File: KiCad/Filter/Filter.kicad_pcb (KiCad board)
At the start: 2 copper layers, 51 x 59 mm, 36 parts, among them J1 Screw_Terminal_01x03, J2 Screw_Terminal_01x03, U1 TL074

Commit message: added silkscreen to help assembly process on all boards
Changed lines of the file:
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@@
 		)
 		(property "Value" "1k"
-			(at 3.81 2.37 0)
+			(at 2 -0.5 0)
 			(layer "F.Fab")
 			(effects
@@
 		)
 		(fp_text user "${REFERENCE}"
-			(at 3.81 0 0)
+			(at 5.5 0.5 0)
 			(layer "F.Fab")
 			(effects
@@
 		(tags "C Rect series Radial pin pitch 15.00mm length 18mm width 5mm Capacitor")
 		(property "Reference" "C3"
-			(at -0.9 -3.75 90)
+			(at -1.15 -3.8 180)
 			(layer "F.SilkS")
 			(effects
@@
 		)
 		(property "Value" "1n"
-			(at 7.5 3.75 90)
-			(layer "F.Fab")
+			(at 7.5 0.2 180)
+			(layer "F.SilkS")
 			(effects
 				(font
@@
 		)
 		(property "Value" "1n"
-			(at 4.5 0 0)
-			(layer "F.Fab")
+			(at 7.5 0 0)
+			(layer "F.SilkS")
 			(effects
 				(font
@@
 		(tags "THT DIP DIL PDIP 2.54mm 7.62mm 300mil")
 		(property "Reference" "U1"
-			(at 3.81 -2.33 90)
+			(at 3.805 -2.63 180)
 			(layer "F.SilkS")
 			(effects
@@
 		)
 		(property "Value" "TL074"
-			(at 3.81 17.57 90)
-			(layer "F.Fab")
+			(at 3.81 7.62 180)
+			(layer "F.SilkS")
 			(effects
 				(font
@@
 		)
 		(property "Value" "1n"
-			(at 7.5 3.75 0)
-			(layer "F.Fab")
+			(at 7.5 0 0)
+			(layer "F.SilkS")
 			(effects
 				(font

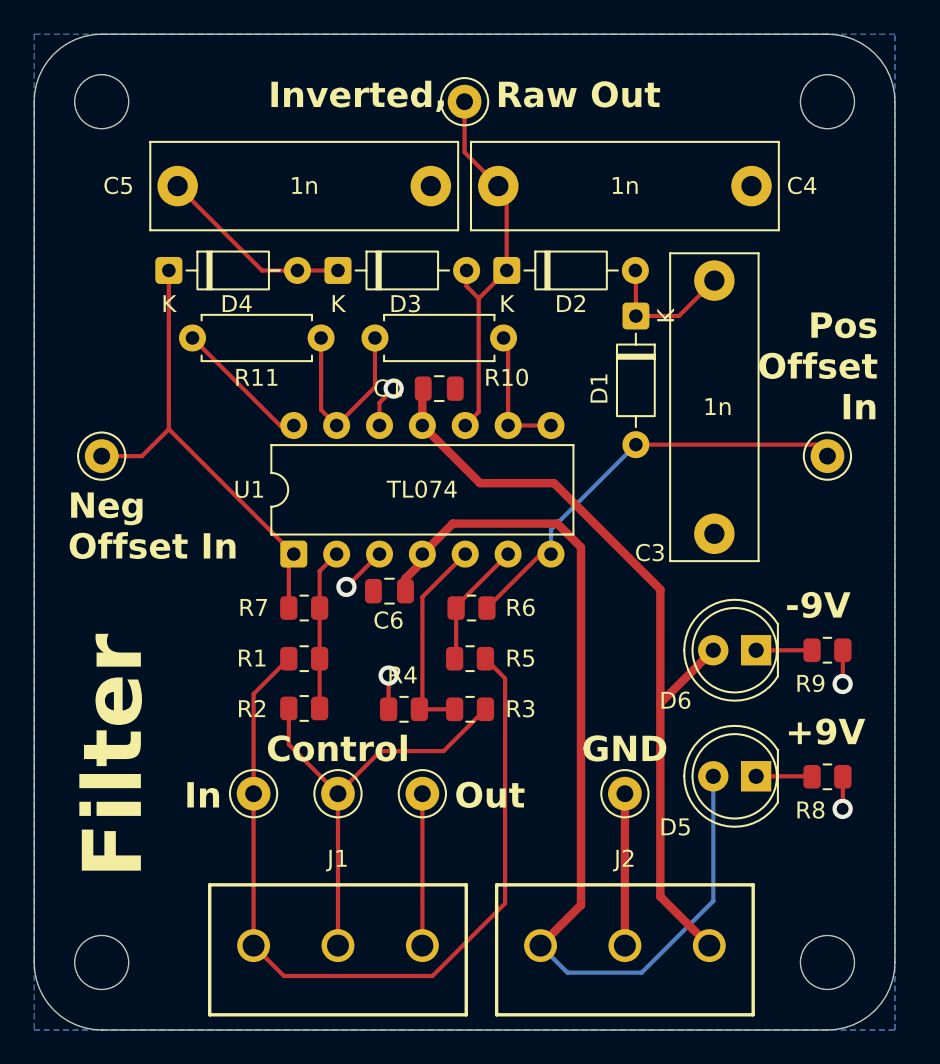
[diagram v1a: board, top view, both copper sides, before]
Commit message: ran DRC on all boards
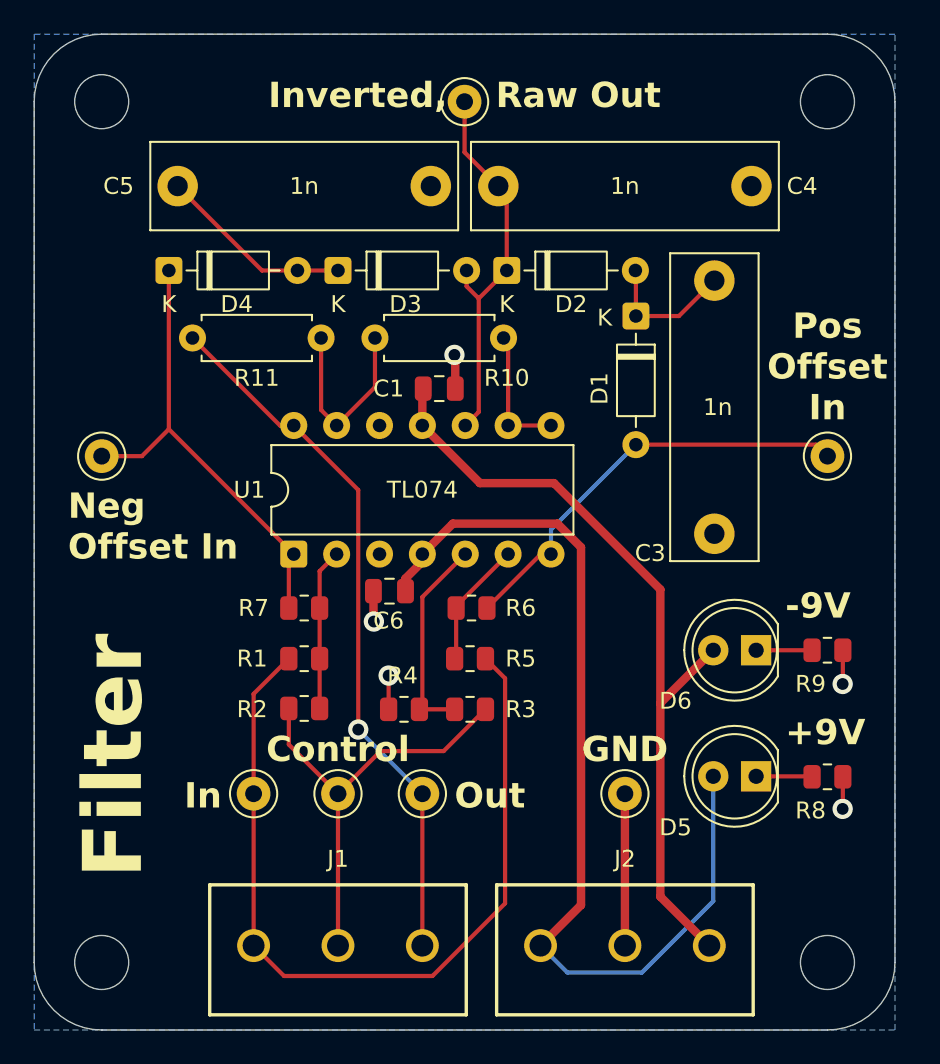
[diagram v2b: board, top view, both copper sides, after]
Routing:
- net /Out: track 17.1 -> 42.3 mm, vias 0 -> 1
- net GND: track 20.2 -> 18.7 mm
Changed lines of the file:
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@@
 			)
 		)
+		(property ki_fp_filters "MountingHole*")
+		(sheetname "/")
+		(sheetfile "Filter.kicad_sch")
+		(units
+			(unit
+				(name "A")
+				(pins)
+			)
+		)
 		(attr exclude_from_pos_files exclude_from_bom)
 		(duplicate_pad_numbers_are_jumpers no)
@@
 			)
 		)
+		(property ki_fp_filters "MountingHole*")
+		(sheetname "/")
+		(sheetfile "Filter.kicad_sch")
+		(units
+			(unit
+				(name "A")
+				(pins)
+			)
+		)
 		(attr exclude_from_pos_files exclude_from_bom)
 		(duplicate_pad_numbers_are_jumpers no)
@@
 			)
 		)
+		(property ki_fp_filters "MountingHole*")
+		(sheetname "/")
+		(sheetfile "Filter.kicad_sch")
+		(units
+			(unit
+				(name "A")
+				(pins)
+			)
+		)
 		(attr exclude_from_pos_files exclude_from_bom)
 		(duplicate_pad_numbers_are_jumpers no)
@@
 		)
 		(fp_text user "K"
-			(at 0 -1.8 90)
+			(at 0.1 1.85 180)
 			(layer "F.SilkS")
 			(effects
@@
 			)
 		)
+		(property ki_fp_filters "MountingHole*")
+		(sheetname "/")
+		(sheetfile "Filter.kicad_sch")
+		(units
+			(unit
+				(name "A")
+				(pins)
+			)
+		)
 		(attr exclude_from_pos_files exclude_from_bom)
 		(duplicate_pad_numbers_are_jumpers no)
@@
 	)
 	(gr_text "Pos\nOffset\nIn"
-		(at 117 67 0)
+		(at 114 67 0)
 		(layer "F.SilkS")
 		(effects
@@
 				(bold yes)
 			)
-			(justify right bottom)
+			(justify bottom)
 		)
 	)
@@
 	)
 	(segment
+		(start 86.2 71.005)
+		(end 82.38 67.185)
+		(width 0.25)
+		(layer "F.Cu")
+		(net "/Out")
+	)
+	(segment
 		(start 81.565 67.185)
 		(end 82.38 67.185)
@@
 	)
 	(segment
+		(start 86.2 85.2)
+		(end 86.2 71.005)
+		(width 0.25)
+		(layer "F.Cu")
+		(net "/Out")
+	)
+	(segment
+		(start 90 89)
+		(end 90.1 88.9)
+		(width 0.25)
+		(layer "F.Cu")
+		(net "/Out")
+	)
+	(segment
 		(start 90 98)
 		(end 90 89)
@@
 		(net "/Out")
 	)
+	(via
+		(at 86.2 85.2)
+		(size 1.2)
+		(drill 0.7)
+		(layers "F.Cu" "B.Cu")
+		(net "/Out")
+	)
+	(segment
+		(start 90 89)
+		(end 86.2 85.2)
+		(width 0.25)
+		(layer "B.Cu")
+		(net "/Out")
+	)
 	(segment
 		(start 94.9 95.5)
@@
 	)
 	(segment
-		(start 87.46 65.84)
-		(end 88.3 65)
-		(width 0.25)
+		(start 91.95 63.05)
+		(end 91.9 63)
+		(width 0.5)
 		(layer "F.Cu")
 		(net "GND")
@@
 	)
 	(segment
-		(start 87.46 67.185)
-		(end 87.46 65.84)
+		(start 114.9125 80.5)
+		(end 114.9125 82.4875)
 		(width 0.25)
 		(layer "F.Cu")
@@
 	)
 	(segment
-		(start 114.9125 80.5)
-		(end 114.9125 82.4875)
-		(width 0.25)
+		(start 91.95 65)
+		(end 91.95 63.05)
+		(width 0.5)
 		(layer "F.Cu")
 		(net "GND")
@@
 	)
 	(segment
-		(start 102 98)
-		(end 102 89)
+		(start 87.1 77)
+		(end 87.1 78.775)
 		(width 0.5)
 		(layer "F.Cu")
@@
 	)
 	(segment
-		(start 85.5 76.75)
-		(end 87.445 74.805)
-		(width 0.25)
+		(start 102 98)
+		(end 102 89)
+		(width 0.5)
 		(layer "F.Cu")
 		(net "GND")
@@
 	)
 	(segment
-		(start 87.445 74.805)
-		(end 87.46 74.805)
-		(width 0.25)
+		(start 87.1 78.775)
+		(end 87.125 78.8)
+		(width 0.5)
 		(layer "F.Cu")
 		(net "GND")
@@
 	)
 	(via
-		(at 85.5 76.75)
+		(at 91.9 63)
 		(size 1.2)
 		(drill 0.7)
@@
 	)
 	(via
-		(at 88 82)
+		(at 87.125 78.8)
 		(size 1.2)
 		(drill 0.7)
@@
 	)
 	(via
-		(at 88.3 65)
+		(at 88 82)
 		(size 1.2)
 		(drill 0.7)

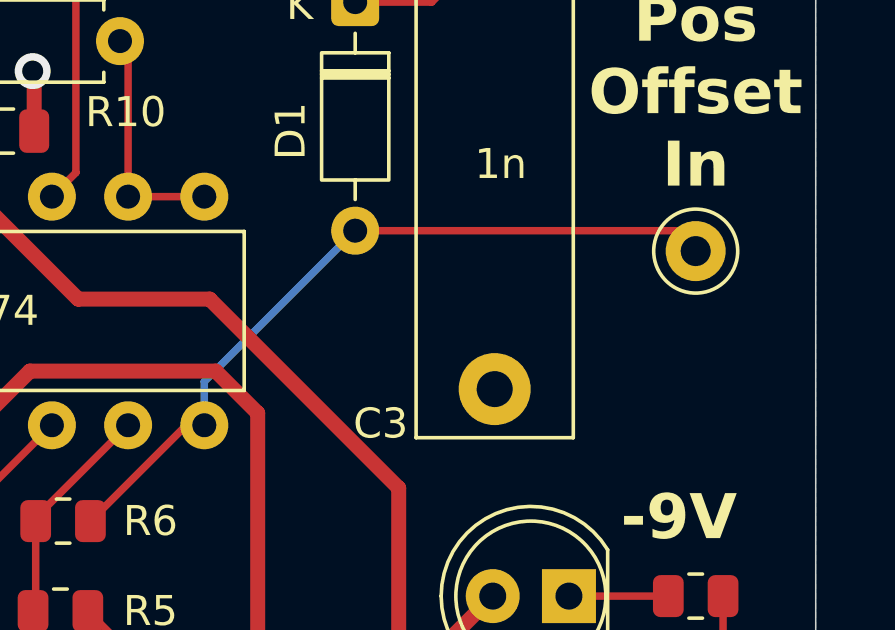
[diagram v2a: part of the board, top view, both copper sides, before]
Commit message: added protection resistor to diode ladder
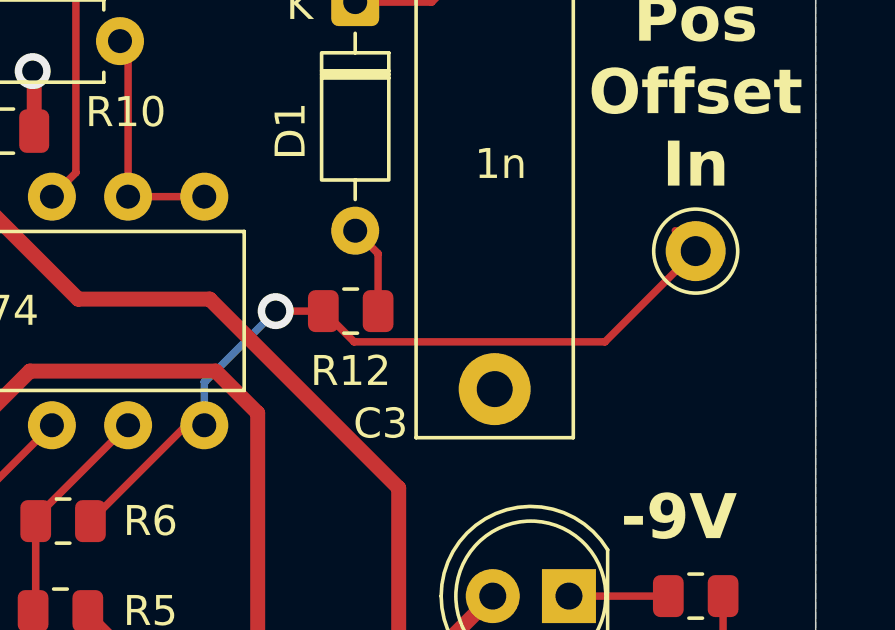
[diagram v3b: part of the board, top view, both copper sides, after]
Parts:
- added R12: 2.2k, Resistor_SMD:R_0805_2012Metric, F.Cu at (102.5, 71.0)
- H1, H2, H3, H4: value MountingHole_3.2mm_M3 -> MountingHole
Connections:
- D1 pad 2: /Signal w. + Offset -> Net-(D1-A)
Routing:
- net Net-(D1-A): track 0.00 -> 3.00 mm
- net /Signal w. + Offset: track 25.3 -> 26.6 mm, vias 0 -> 1
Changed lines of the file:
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@@
 			)
 		)
-		(property "Value" "MountingHole_3.2mm_M3"
+		(property "Value" "MountingHole"
 			(at 0 4.15 0)
 			(layer "F.Fab")
@@
 			)
 		)
-		(property "Description" ""
+		(property "Description" "Mounting Hole without connection"
 			(at 0 0 0)
 			(layer "F.Fab")
@@
 			)
 		)
-		(attr exclude_from_pos_files exclude_from_bom)
+		(attr exclude_from_bom)
 		(duplicate_pad_numbers_are_jumpers no)
 		(fp_circle
@@
 			)
 		)
-		(property "Value" "MountingHole_3.2mm_M3"
+		(property "Value" "MountingHole"
 			(at 0 4.15 0)
 			(layer "F.Fab")
@@
 			)
 		)
-		(property "Description" ""
+		(property "Description" "Mounting Hole without connection"
 			(at 0 0 0)
 			(layer "F.Fab")
@@
 			)
 		)
-		(attr exclude_from_pos_files exclude_from_bom)
+		(attr exclude_from_bom)
 		(duplicate_pad_numbers_are_jumpers no)
 		(fp_circle
@@
 		)
 	)
+	(footprint "Resistor_SMD:R_0805_2012Metric"
+		(layer "F.Cu")
+		(at 102.5 71)
+		(descr "Resistor SMD 0805 (2012 Metric), square (rectangular) end terminal, IPC-7351 nominal, (Body size source: IPC-SM-782 page 72, https://www.pcb-3d.com/wordpress/wp-content/uploads/ipc-sm-782a_amendment_1_and_2.pdf)")
+		(tags "resistor")
+		(property "Reference" "R12"
+			(at 0 2 0)
+			(layer "F.SilkS")
+			(effects
+				(font
+					(size 1 1)
+					(thickness 0.15)
+				)
+			)
+		)
+		(property "Value" "2.2k"
+			(at 0 1.65 0)
+			(layer "F.Fab")
+			(effects
+				(font
+					(size 1 1)
+					(thickness 0.15)
+				)
+			)
+		)
+		(property "Datasheet" ""
+			(at 0 0 0)
+			(layer "F.Fab")
+			(hide yes)
+			(effects
+				(font
+					(size 1.27 1.27)
+				)
+			)
+		)
+		(property "Description" "Resistor, US symbol"
+			(at 0 0 0)
+			(layer "F.Fab")
+			(hide yes)
+			(effects
+				(font
+					(size 1.27 1.27)
+				)
+			)
+		)
+		(property "KiLib_Generator" "SMD_2terminal_chip_molded"
+			(at 0 0 0)
+			(layer "F.SilkS")
+			(hide yes)
+			(effects
+				(font
+					(size 1 1)
+					(thickness 0.15)
+				)
+			)
+		)
+		(property "LCSC Part #" ""
+			(at 0 0 0)
+			(unlocked yes)
+			(layer "F.Fab")
+			(hide yes)
+			(effects
+				(font
+					(size 1 1)
+					(thickness 0.15)
+				)
+			)
+		)
+		(property ki_fp_filters "R_*")
+		(sheetname "/")
+		(sheetfile "Filter.kicad_sch")
+		(units
+			(unit
+				(name "A")
+				(pins "1" "2")
+			)
+		)
+		(attr smd)
+		(duplicate_pad_numbers_are_jumpers no)
+		(fp_line
+			(start -0.227064 -0.735)
+			(end 0.227064 -0.735)
+			(stroke
+				(width 0.12)
+				(type solid)
+			)
+			(layer "F.SilkS")
+		)
+		(fp_line
+			(start -0.227064 0.735)
+			(end 0.227064 0.735)
+			(stroke
+				(width 0.12)
+				(type solid)
+			)
+			(layer "F.SilkS")
+		)
+		(fp_rect
+			(start -1.68 -0.95)
+			(end 1.68 0.95)
+			(stroke
+				(width 0.05)
+				(type solid)
+			)
+			(fill no)
+			(layer "F.CrtYd")
+		)
+		(fp_rect
+			(start -1 -0.625)
+			(end 1 0.625)
+			(stroke
+				(width 0.1)
+				(type solid)
+			)
+			(fill no)
+			(layer "F.Fab")
+		)
+		(fp_text user "${REFERENCE}"
+			(at 0 0 0)
+			(layer "F.Fab")
+			(effects
+				(font
+					(size 0.5 0.5)
+					(thickness 0.08)
+				)
+			)
+		)
+		(pad "1" smd roundrect
+			(at -0.9125 0)
+			(size 1.025 1.4)
+			(layers "F.Cu" "F.Mask" "F.Paste")
+			(roundrect_rratio 0.243902)
+			(net "/Signal w. + Offset")
+			(pintype "passive")
+		)
+		(pad "2" smd roundrect
+			(at 0.9125 0)
+			(size 1.025 1.4)
+			(layers "F.Cu" "F.Mask" "F.Paste")
+			(roundrect_rratio 0.243902)
+			(net "Net-(D1-A)")
+			(pintype "passive")
+		)
+		(embedded_fonts no)
+		(model "${KICAD10_3DMODEL_DIR}/Resistor_SMD.3dshapes/R_0805_2012Metric.step"
+			(offset
+				(xyz 0 0 0)
+			)
+			(scale
+				(xyz 1 1 1)
+			)
+			(rotate
+				(xyz 0 0 0)
+			)
+		)
+	)
 	(footprint "Diode_THT:D_DO-35_SOD27_P7.62mm_Horizontal"
 		(layer "F.Cu")
@@
 			)
 		)
-		(property "Value" "MountingHole_3.2mm_M3"
+		(property "Value" "MountingHole"
 			(at 0 4.15 0)
 			(layer "F.Fab")
@@
 			)
 		)
-		(property "Description" ""
+		(property "Description" "Mounting Hole without connection"
 			(at 0 0 0)
 			(layer "F.Fab")
@@
 			)
 		)
-		(attr exclude_from_pos_files exclude_from_bom)
+		(attr exclude_from_bom)
 		(duplicate_pad_numbers_are_jumpers no)
 		(fp_circle
@@
 			(layers "*.Cu" "*.Mask")
 			(remove_unused_layers no)
-			(net "/Signal w. + Offset")
+			(net "Net-(D1-A)")
 			(pinfunction "A_2")
 			(pintype "passive")
@@
 			)
 		)
-		(property "Value" "MountingHole_3.2mm_M3"
+		(property "Value" "MountingHole"
 			(at 0 4.15 0)
 			(layer "F.Fab")
@@
 			)
 		)
-		(property "Description" ""
+		(property "Description" "Mounting Hole without connection"
 			(at 0 0 0)
 			(layer "F.Fab")
@@
 			)
 		)
-		(attr exclude_from_pos_files exclude_from_bom)
+		(attr exclude_from_bom)
 		(duplicate_pad_numbers_are_jumpers no)
 		(fp_circle
@@
 	)
 	(segment
-		(start 102.65 68.32)
-		(end 113.32 68.32)
+		(start 113.32 68.32)
+		(end 114 69)
 		(width 0.25)
 		(layer "F.Cu")
@@
 	)
 	(segment
-		(start 113.32 68.32)
-		(end 114 69)
+		(start 100 71)
+		(end 101.5875 71)
+		(width 0.25)
+		(layer "F.Cu")
+		(net "/Signal w. + Offset")
+	)
+	(segment
+		(start 101.5875 71)
+		(end 102.6125 72.025)
 		(width 0.25)
 		(layer "F.Cu")
@@
 	)
 	(segment
+		(start 102.6125 72.025)
+		(end 110.975 72.025)
+		(width 0.25)
+		(layer "F.Cu")
+		(net "/Signal w. + Offset")
+	)
+	(segment
 		(start 93.825 78)
 		(end 97.02 74.805)
@@
 	)
 	(segment
-		(start 97.62 73.35)
-		(end 102.65 68.32)
+		(start 110.975 72.025)
+		(end 114 69)
+		(width 0.25)
+		(layer "F.Cu")
+		(net "/Signal w. + Offset")
+	)
+	(via
+		(at 100 71)
+		(size 1.2)
+		(drill 0.7)
+		(layers "F.Cu" "B.Cu")
+		(net "/Signal w. + Offset")
+	)
+	(segment
+		(start 97.65 73.35)
+		(end 100 71)
 		(width 0.25)
 		(layer "B.Cu")
@@
 	)
 	(segment
+		(start 97.62 73.35)
+		(end 97.65 73.35)
+		(width 0.25)
+		(layer "B.Cu")
+		(net "/Signal w. + Offset")
+	)
+	(segment
 		(start 92 77.885)
 		(end 95.08 74.805)
@@
 		(net "Net-(U1B--)")
 	)
+	(segment
+		(start 103.4125 69.0825)
+		(end 102.65 68.32)
+		(width 0.25)
+		(layer "F.Cu")
+		(net "Net-(D1-A)")
+	)
+	(segment
+		(start 103.4125 71)
+		(end 103.4125 69.0825)
+		(width 0.25)
+		(layer "F.Cu")
+		(net "Net-(D1-A)")
+	)
 	(zone

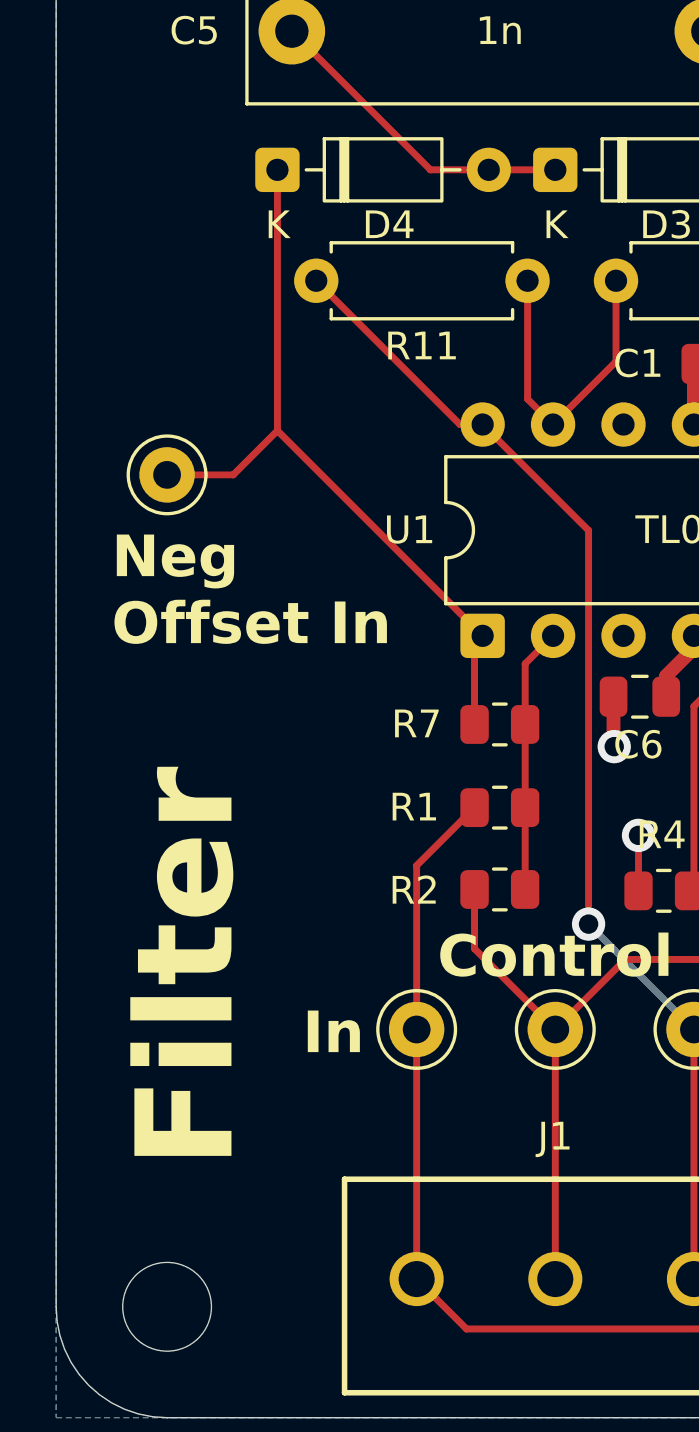
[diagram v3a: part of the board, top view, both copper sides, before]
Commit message: added graphics to some boards
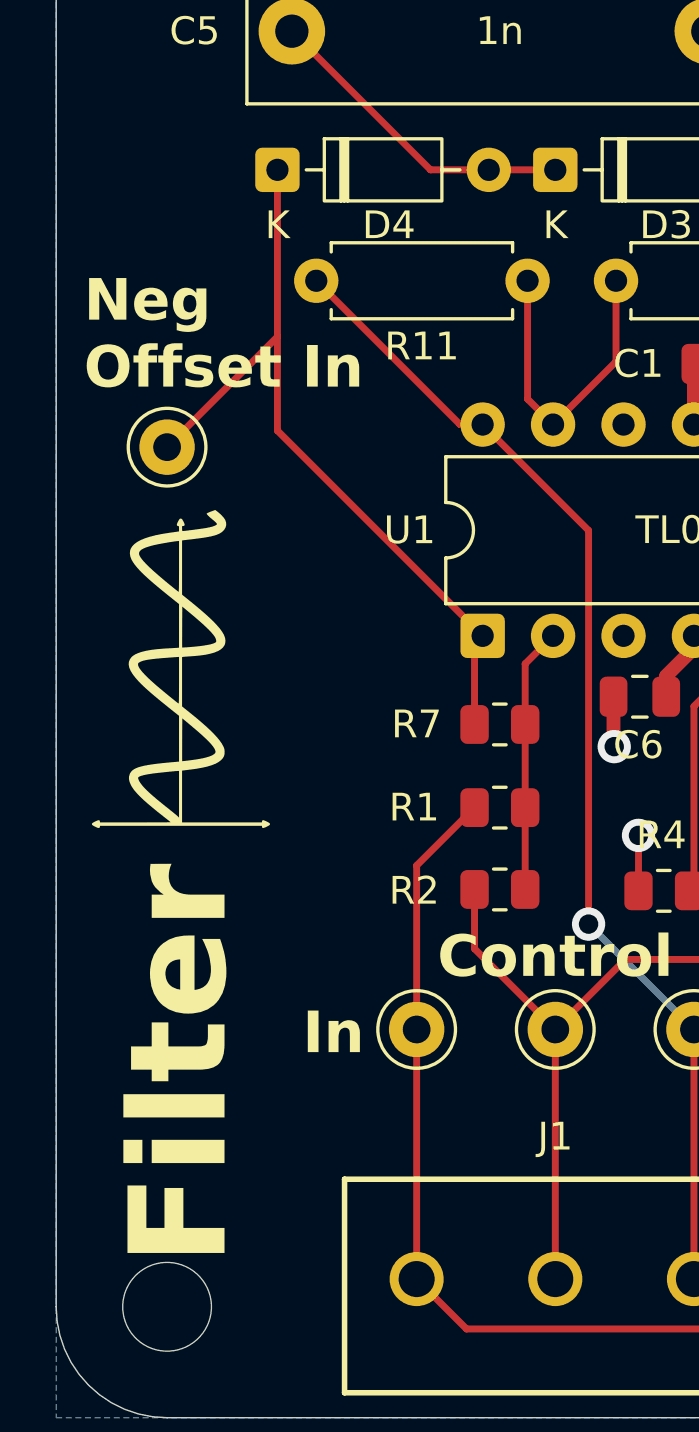
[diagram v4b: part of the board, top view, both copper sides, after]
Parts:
- added G***: LOGO, LOGO, F.Cu at (71.4, 74.6)
- moved TP6 1.00 mm to (71.0, 68.0)
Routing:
- net /Signal w. - Offset: track 27.8 -> 28.8 mm
